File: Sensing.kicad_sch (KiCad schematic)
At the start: 86 parts, among them IC1 LM358BIDDFR, IC10 H11L1SM, IC11 LM358BIDDFR, IC12 H11L1SM, IC2 H11L1SM, IC3 LM358BIDDFR, IC4 H11L1SM, IC5 LM358BIDDFR, IC6 H11L1SM, IC7 LM358BIDDFR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

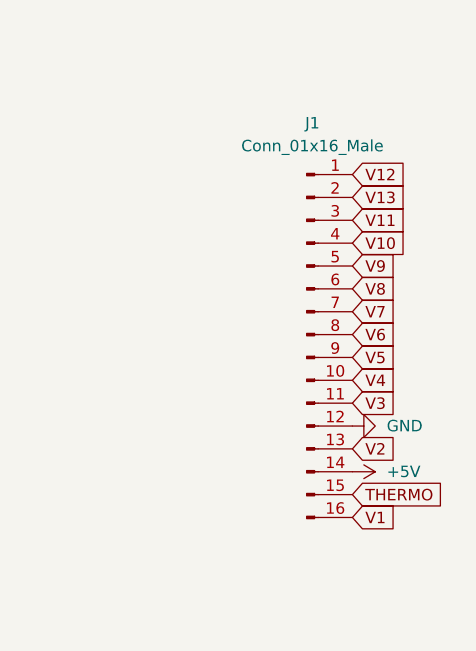
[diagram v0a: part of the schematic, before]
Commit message: added shorter connector
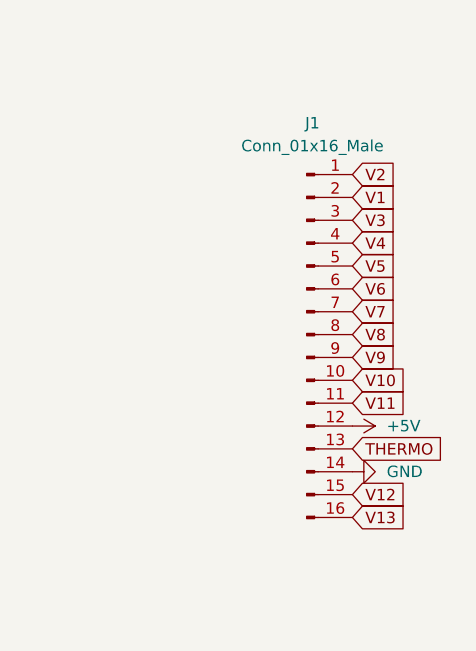
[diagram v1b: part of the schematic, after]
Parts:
- J1: footprint Connector_Hirose:Hirose_DF11-16DP-2DSA_2x08_P2.00mm_Vertical -> KiCad:117347426
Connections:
- net +5V: now also J1.12 (Pin_12); no longer J1.14 (Pin_14)
- net GND: now also J1.14 (Pin_14); no longer J1.12 (Pin_12)
- net THERMO: now also J1.13 (Pin_13); no longer J1.15 (Pin_15)
- net V1: now also J1.2 (Pin_2); no longer J1.16 (Pin_16)
- net V10: now also J1.10 (Pin_10); no longer J1.4 (Pin_4)
- net V11: now also J1.11 (Pin_11); no longer J1.3 (Pin_3)
- net V12: now also J1.15 (Pin_15); no longer J1.1 (Pin_1)
- net V13: now also J1.16 (Pin_16); no longer J1.2 (Pin_2)
- net V2: now also J1.1 (Pin_1); no longer J1.13 (Pin_13)
- net V3: now also J1.3 (Pin_3); no longer J1.11 (Pin_11)
- net V4: now also J1.4 (Pin_4); no longer J1.10 (Pin_10)
- net V5: now also J1.5 (Pin_5); no longer J1.9 (Pin_9)
- net V6: now also J1.6 (Pin_6); no longer J1.8 (Pin_8)
- net V8: now also J1.8 (Pin_8); no longer J1.6 (Pin_6)
- net V9: now also J1.9 (Pin_9); no longer J1.5 (Pin_5)
